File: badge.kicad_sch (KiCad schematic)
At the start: 0 parts

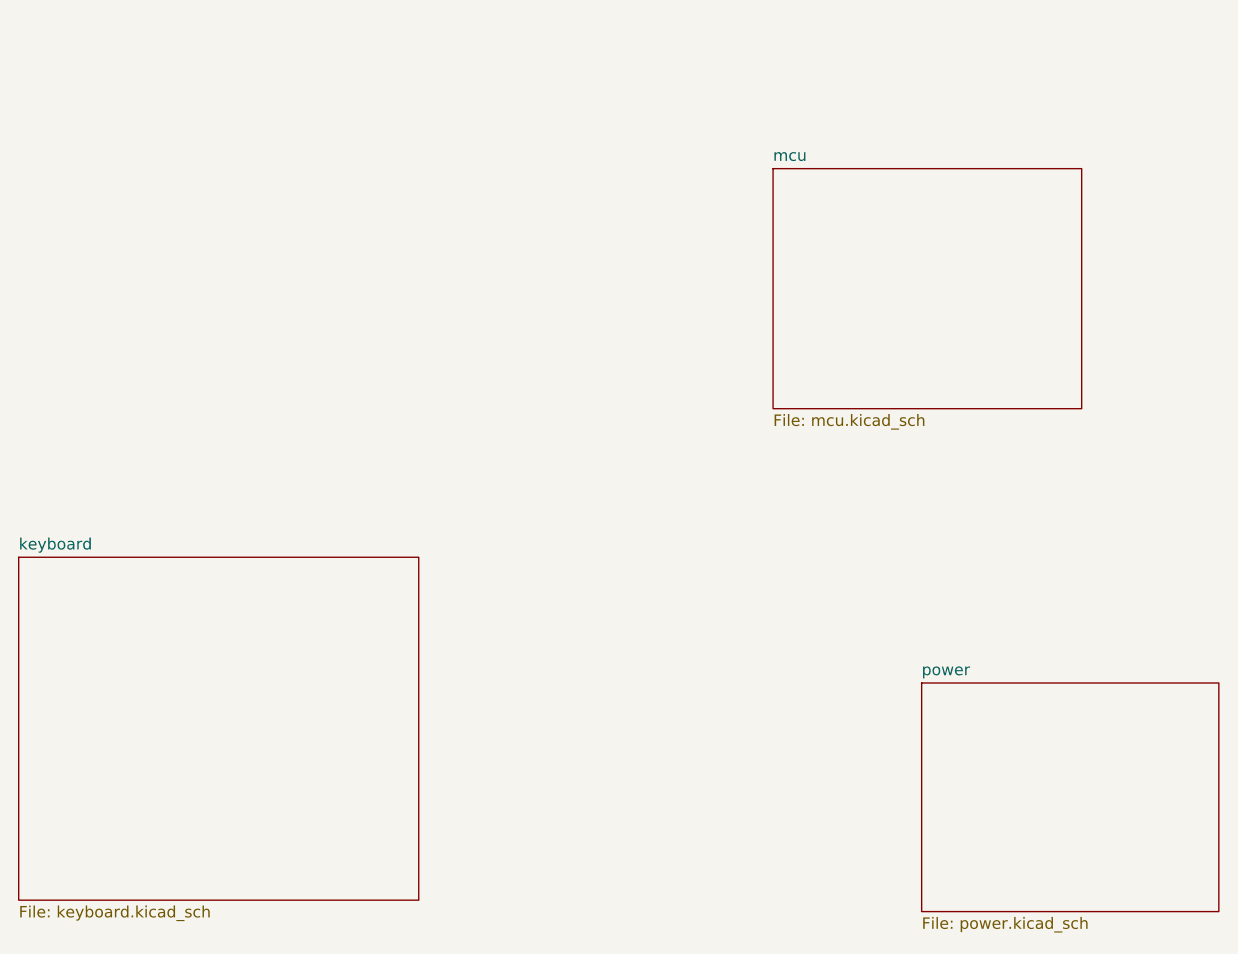
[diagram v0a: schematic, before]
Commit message: add sensors sheet
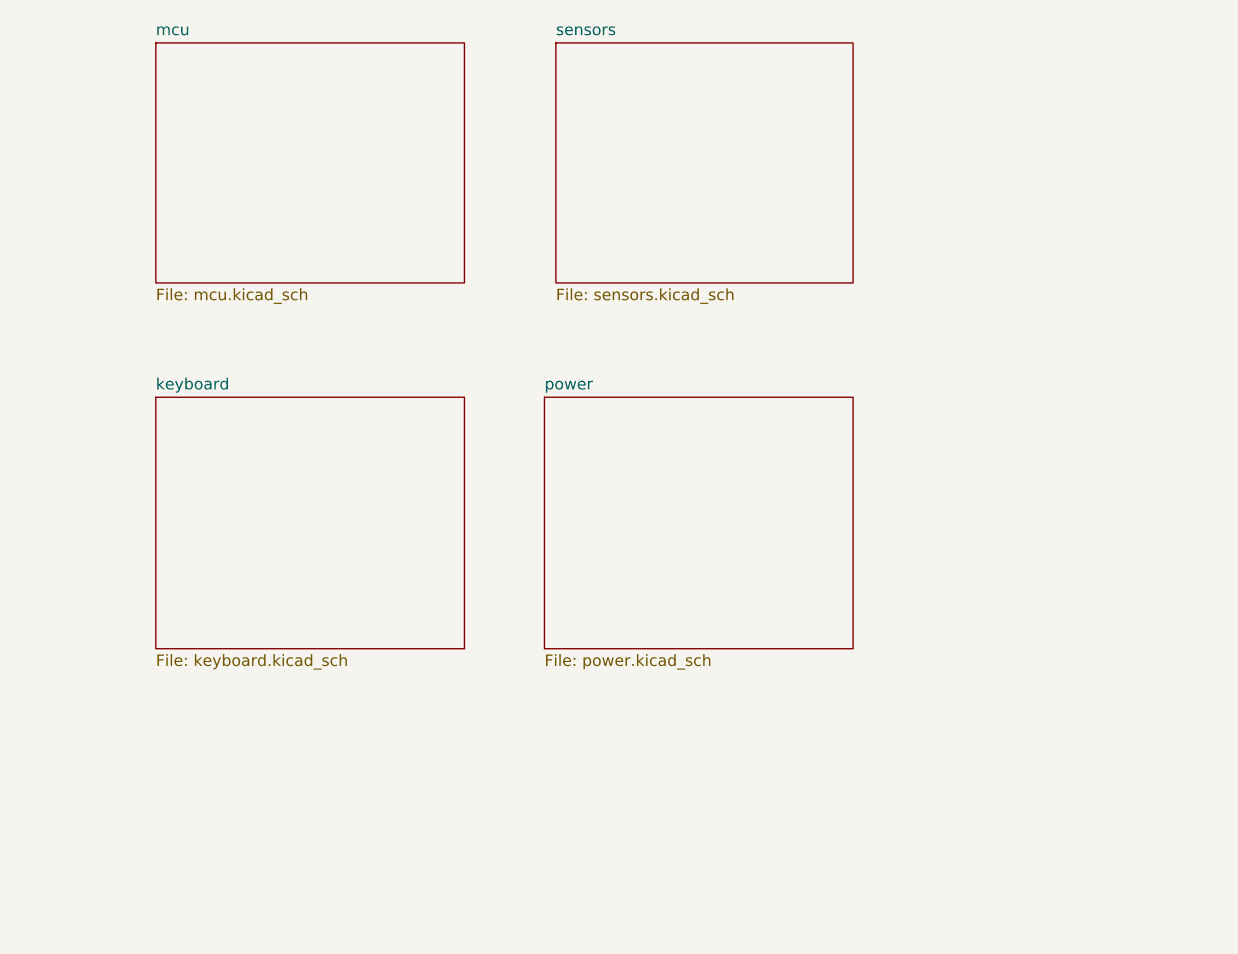
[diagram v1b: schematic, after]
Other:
- added sheet sensors (sensors.kicad_sch)
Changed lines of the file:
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@@
 	(paper "A4")
 	(sheet
-		(at 62.23 104.14)
-		(size 44.45 38.1)
+		(at 77.47 86.36)
+		(size 34.29 27.94)
 		(fields_autoplaced yes)
 		(stroke
@@
 		)
 		(property "Sheetname" "keyboard"
-			(at 62.23 103.4284 0)
+			(at 77.47 85.6484 0)
 			(effects
 				(font
@@
 		)
 		(property "Sheetfile" "keyboard.kicad_sch"
-			(at 62.23 142.8246 0)
+			(at 77.47 114.8846 0)
 			(effects
 				(font
@@
 	)
 	(sheet
-		(at 146.05 60.96)
+		(at 77.47 46.99)
 		(size 34.29 26.67)
 		(fields_autoplaced yes)
@@
 		)
 		(property "Sheetname" "mcu"
-			(at 146.05 60.2484 0)
+			(at 77.47 46.2784 0)
 			(effects
 				(font
@@
 		)
 		(property "Sheetfile" "mcu.kicad_sch"
-			(at 146.05 88.2146 0)
+			(at 77.47 74.2446 0)
 			(effects
 				(font
@@
 	)
 	(sheet
-		(at 162.56 118.11)
-		(size 33.02 25.4)
+		(at 121.92 46.99)
+		(size 33.02 26.67)
+		(fields_autoplaced yes)
+		(stroke
+			(width 0.1524)
+			(type solid)
+		)
+		(fill
+			(color 0 0 0 0.0000)
+		)
+		(property "Sheetname" "sensors"
+			(at 121.92 46.2784 0)
+			(effects
+				(font
+					(size 1.27 1.27)
+				)
+				(justify left bottom)
+			)
+		)
+		(property "Sheetfile" "sensors.kicad_sch"
+			(at 121.92 74.2446 0)
+			(effects
+				(font
+					(size 1.27 1.27)
+				)
+				(justify left top)
+			)
+		)
+		(instances
+			(project "badge"
+				(path "/dc4a3d77-b0f8-4e90-a4be-3e93c7025348"
+					(page "5")
+				)
+			)
+		)
+	)
+	(sheet
+		(at 120.65 86.36)
+		(size 34.29 27.94)
 		(fields_autoplaced yes)
 		(stroke
@@
 		)
 		(property "Sheetname" "power"
-			(at 162.56 117.3984 0)
+			(at 120.65 85.6484 0)
 			(effects
 				(font
@@
 		)
 		(property "Sheetfile" "power.kicad_sch"
-			(at 162.56 144.0946 0)
+			(at 120.65 114.8846 0)
 			(effects
 				(font
